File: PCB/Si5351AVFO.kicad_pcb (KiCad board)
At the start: 4 copper layers, 100 x 65 mm, 133 parts, among them J1 USB_C_Receptacle, J2 SMA CLK0, J3 SMA CLK1, J4 SMA CLK2, J5 UPDI, SW1 EC11E18244A5, SW2 SOFT1, SW3 SOFT2, SW4 SOFT3, U1 LP2985-3.3, U2 Si5351A-B-GT, U3 CP2102N-A02-GQFN24, U4 ATtiny3226-SU, U5 LP2985-3.3, X1 25MHz TCXO

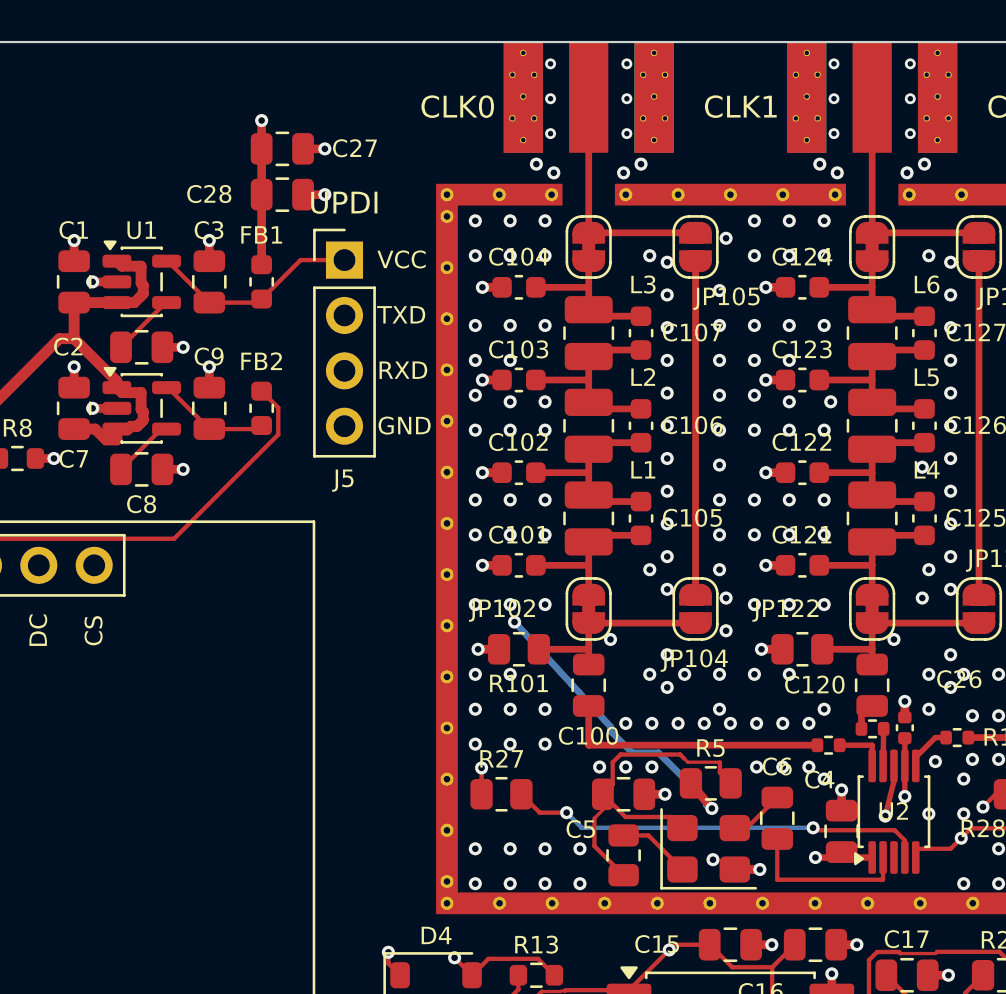
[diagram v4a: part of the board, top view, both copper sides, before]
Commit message: PCB silk nits: C4 0.3 mm off U2 (no silk overlap), C27/C28 mirrored west of +3V3_CLK trunk clear of UPDI legend; DRC: only SMA edge-launch hits
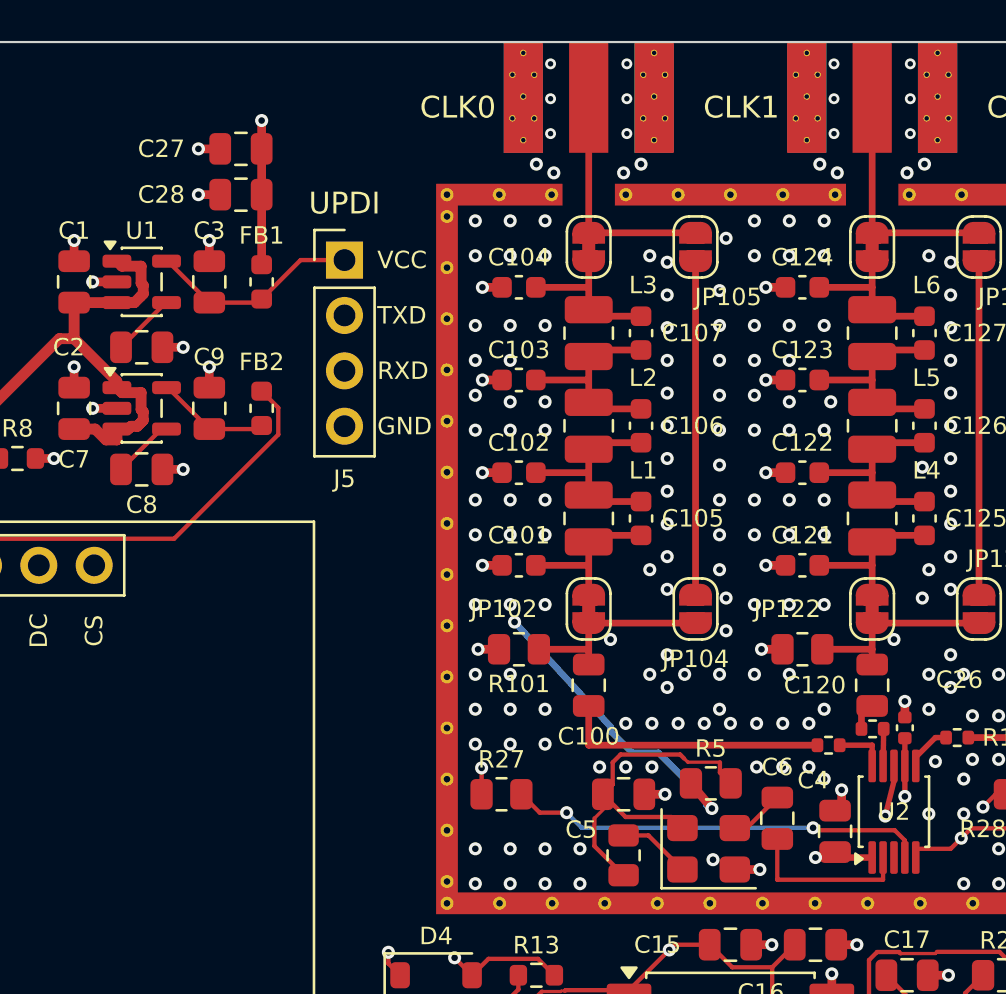
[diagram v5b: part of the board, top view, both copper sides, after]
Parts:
- moved C27 1.90 mm to (142.1, 104.9), turned to 180 degrees
- moved C28 1.90 mm to (142.1, 107.0), turned to 180 degrees
- moved C4 0.30 mm to (169.3, 136.2)
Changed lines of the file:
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@@
 	(footprint "Capacitor_SMD:C_0805_2012Metric"
 		(layer "F.Cu")
-		(at 143.95 104.9)
+		(at 142.05 104.9 180)
 		(descr "Capacitor SMD 0805 (2012 Metric), square (rectangular) end terminal, IPC-7351 nominal, (Body size source: IPC-SM-782 page 76, https://www.pcb-3d.com/wordpress/wp-content/uploads/ipc-sm-782a_amendment_1_and_2.pdf, https://docs.google.com/spreadsheets/d/1BsfQQcO9C6DZCsRaXUlFlo91Tg2WpOkGARC1WS5S8t0/edit?usp=sharing)")
 		(tags "capacitor")
 		(property "Reference" "C27"
-			(at 3.344999 0 0)
+			(at 3.65 0 0)
 			(layer "F.SilkS")
 			(effects
@@
 		)
 		(property "Value" "10u"
-			(at 0 1.68 0)
+			(at 0 1.68 180)
 			(layer "F.Fab")
 			(hide yes)
@@
 		)
 		(property "Datasheet" ""
-			(at 0 0 0)
+			(at 0 0 180)
 			(layer "F.Fab")
 			(hide yes)
@@
 		)
 		(property "Description" "Unpolarized capacitor, small symbol"
-			(at 0 0 0)
+			(at 0 0 180)
 			(layer "F.Fab")
 			(hide yes)
@@
 		)
 		(property "KiLib_Generator" "SMD_2terminal_chip_molded"
-			(at 0 0 0)
+			(at 0 0 180)
 			(layer "F.SilkS")
 			(hide yes)
@@
 		)
 		(property "LCSC" "C15850"
-			(at 0 0 0)
+			(at 0 0 180)
 			(layer "F.SilkS")
 			(hide yes)
@@
 		)
 		(property "MPN" "CL21A106KAYNNNE"
-			(at 0 0 0)
+			(at 0 0 180)
 			(layer "F.SilkS")
 			(hide yes)
@@
 		)
 		(property "Manufacturer" "Samsung Electro-Mechanics"
-			(at 0 0 0)
+			(at 0 0 180)
 			(layer "F.SilkS")
 			(hide yes)
@@
 		(duplicate_pad_numbers_are_jumpers no)
 		(fp_line
-			(start -0.261252 -0.735)
-			(end 0.261252 -0.735)
+			(start -0.261252 0.735)
+			(end 0.261252 0.735)
 			(stroke
 				(width 0.12)
@@
 		)
 		(fp_line
-			(start -0.261252 0.735)
-			(end 0.261252 0.735)
+			(start -0.261252 -0.735)
+			(end 0.261252 -0.735)
 			(stroke
 				(width 0.12)
@@
 		)
 		(fp_text user "${REFERENCE}"
-			(at 0 0 0)
+			(at 0 0 180)
 			(layer "F.Fab")
 			(effects
@@
 		)
 		(pad "1" smd roundrect
-			(at -0.95 0)
+			(at -0.95 0 180)
 			(size 1 1.45)
 			(layers "F.Cu" "F.Mask" "F.Paste")
@@
 		)
 		(pad "2" smd roundrect
-			(at 0.95 0)
+			(at 0.95 0 180)
 			(size 1 1.45)
 			(layers "F.Cu" "F.Mask" "F.Paste")
@@
 	(footprint "Capacitor_SMD:C_0805_2012Metric"
 		(layer "F.Cu")
-		(at 143.95 107)
+		(at 142.05 107 180)
 		(descr "Capacitor SMD 0805 (2012 Metric), square (rectangular) end terminal, IPC-7351 nominal, (Body size source: IPC-SM-782 page 76, https://www.pcb-3d.com/wordpress/wp-content/uploads/ipc-sm-782a_amendment_1_and_2.pdf, https://docs.google.com/spreadsheets/d/1BsfQQcO9C6DZCsRaXUlFlo91Tg2WpOkGARC1WS5S8t0/edit?usp=sharing)")
 		(tags "capacitor")
 		(property "Reference" "C28"
-			(at -3.345 0 0)
+			(at 3.65 0 0)
 			(layer "F.SilkS")
 			(effects
@@
 		)
 		(property "Value" "100n"
-			(at 0 1.68 0)
+			(at 0 1.68 180)
 			(layer "F.Fab")
 			(hide yes)
@@
 		)
 		(property "Datasheet" ""
-			(at 0 0 0)
+			(at 0 0 180)
 			(layer "F.Fab")
 			(hide yes)
@@
 		)
 		(property "Description" "Unpolarized capacitor, small symbol"
-			(at 0 0 0)
+			(at 0 0 180)
 			(layer "F.Fab")
 			(hide yes)
@@
 		)
 		(property "KiLib_Generator" "SMD_2terminal_chip_molded"
-			(at 0 0 0)
+			(at 0 0 180)
 			(layer "F.SilkS")
 			(hide yes)
@@
 		)
 		(property "LCSC" "C49678"
-			(at 0 0 0)
+			(at 0 0 180)
 			(layer "F.SilkS")
 			(hide yes)
@@
 		)
 		(property "MPN" "CC0805KRX7R9BB104"
-			(at 0 0 0)
+			(at 0 0 180)
 			(layer "F.SilkS")
 			(hide yes)
@@
 		)
 		(property "Manufacturer" "YAGEO"
-			(at 0 0 0)
+			(at 0 0 180)
 			(layer "F.SilkS")
 			(hide yes)
@@
 		(duplicate_pad_numbers_are_jumpers no)
 		(fp_line
-			(start -0.261252 -0.735)
-			(end 0.261252 -0.735)
+			(start -0.261252 0.735)
+			(end 0.261252 0.735)
 			(stroke
 				(width 0.12)
@@
 		)
 		(fp_line
-			(start -0.261252 0.735)
-			(end 0.261252 0.735)
+			(start -0.261252 -0.735)
+			(end 0.261252 -0.735)
 			(stroke
 				(width 0.12)
@@
 		)
 		(fp_text user "${REFERENCE}"
-			(at 0 0 0)
+			(at 0 0 180)
 			(layer "F.Fab")
 			(effects
@@
 		)
 		(pad "1" smd roundrect
-			(at -0.95 0)
+			(at -0.95 0 180)
 			(size 1 1.45)
 			(layers "F.Cu" "F.Mask" "F.Paste")
@@
 		)
 		(pad "2" smd roundrect
-			(at 0.95 0)
+			(at 0.95 0 180)
 			(size 1 1.45)
 			(layers "F.Cu" "F.Mask" "F.Paste")
@@
 	(footprint "Capacitor_SMD:C_0805_2012Metric"
 		(layer "F.Cu")
-		(at 169.6 136.2 90)
+		(at 169.3 136.2 90)
 		(descr "Capacitor SMD 0805 (2012 Metric), square (rectangular) end terminal, IPC-7351 nominal, (Body size source: IPC-SM-782 page 76, https://www.pcb-3d.com/wordpress/wp-content/uploads/ipc-sm-782a_amendment_1_and_2.pdf, https://docs.google.com/spreadsheets/d/1BsfQQcO9C6DZCsRaXUlFlo91Tg2WpOkGARC1WS5S8t0/edit?usp=sharing)")
 		(tags "capacitor")
@@
 	)
 	(segment
-		(start 144.9 107)
-		(end 145.9 107)
-		(width 0.4)
-		(layer "F.Cu")
-		(net "GND")
-	)
-	(segment
 		(start 138.45 114)
 		(end 139.399999 114)
@@
 	)
 	(segment
+		(start 141.1 107)
+		(end 140.1 107)
+		(width 0.4)
+		(layer "F.Cu")
+		(net "GND")
+	)
+	(segment
+		(start 141.1 104.9)
+		(end 140.1 104.9)
+		(width 0.4)
+		(layer "F.Cu")
+		(net "GND")
+	)
+	(segment
 		(start 183.25 136.6)
 		(end 184.2 136.6)
@@
 	)
 	(segment
-		(start 144.9 104.9)
-		(end 145.9 104.9)
-		(width 0.4)
-		(layer "F.Cu")
-		(net "GND")
-	)
-	(segment
 		(start 136.2 163.25)
 		(end 134.75 163.25)
@@
 	)
 	(via
+		(at 140.1 104.9)
+		(size 0.6)
+		(drill 0.3)
+		(layers "F.Cu" "B.Cu")
+		(net "GND")
+	)
+	(via
 		(at 179.999999 121)
 		(size 0.6)
@@
 	)
 	(via
-		(at 145.9 104.9)
-		(size 0.6)
-		(drill 0.3)
-		(layers "F.Cu" "B.Cu")
-		(net "GND")
-	)
-	(via
 		(at 179.999999 117.8)
 		(size 0.6)
@@
 	)
 	(via
-		(at 145.9 107)
-		(size 0.6)
-		(drill 0.3)
-		(layers "F.Cu" "B.Cu")
-		(net "GND")
-	)
-	(via
 		(at 165.6 117.8)
 		(size 0.6)
@@
 		(net "GND")
 	)
+	(via
+		(at 140.1 107)
+		(size 0.6)
+		(drill 0.3)
+		(layers "F.Cu" "B.Cu")
+		(net "GND")
+	)
 	(segment
 		(start 187 102.5)
@@
 	)
 	(segment
-		(start 169.6 137.4)
+		(start 169.3 137.4)
 		(end 171 137.4)
 		(width 0.3)
@@
 	(segment
 		(start 168.4 137.4)
-		(end 169.6 137.4)
+		(end 169.3 137.4)
 		(width 0.3)
 		(locked yes)
